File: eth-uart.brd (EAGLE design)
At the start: 52 x 21 mm, 41 parts, among them IC1 STM32F407VE, IC2 DP83848, IC3 LDS3985M33R, X5 USBMICRO_B, X7 B78477P1001A314

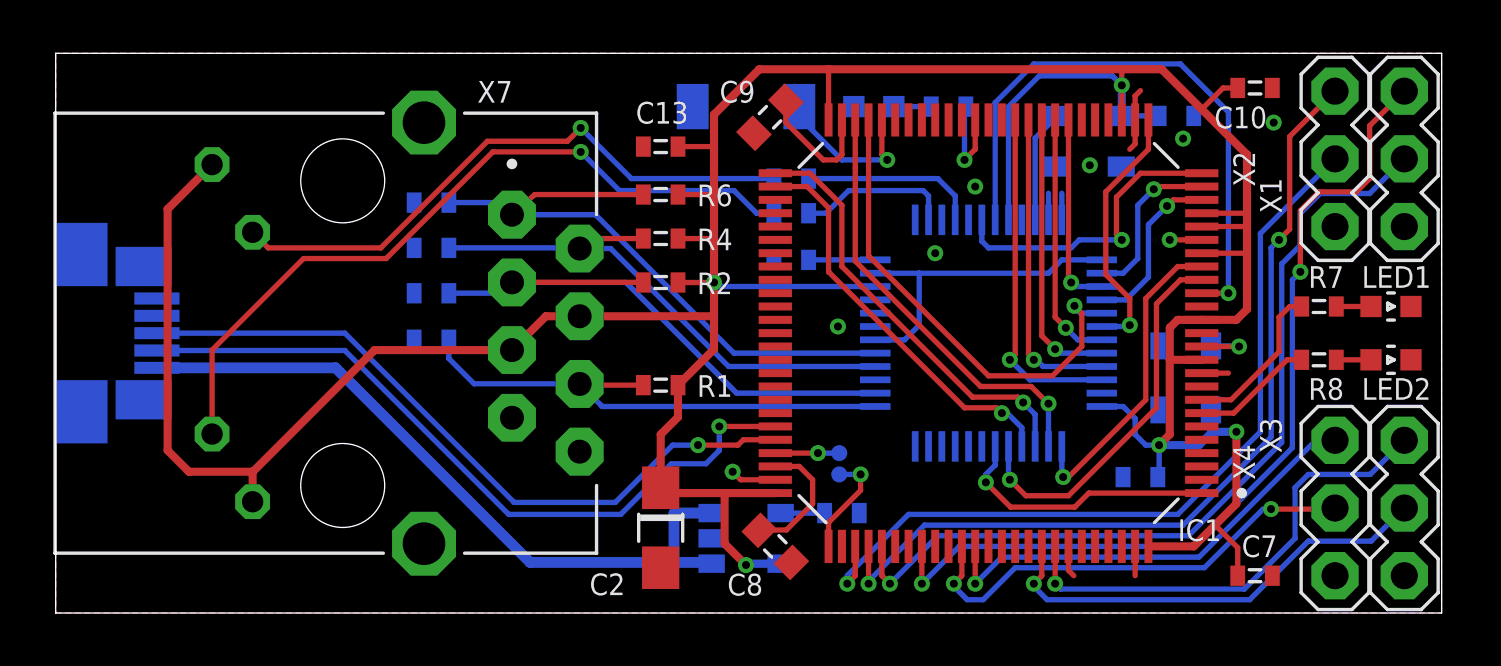
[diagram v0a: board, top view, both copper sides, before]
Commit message: boot0 on solidjump
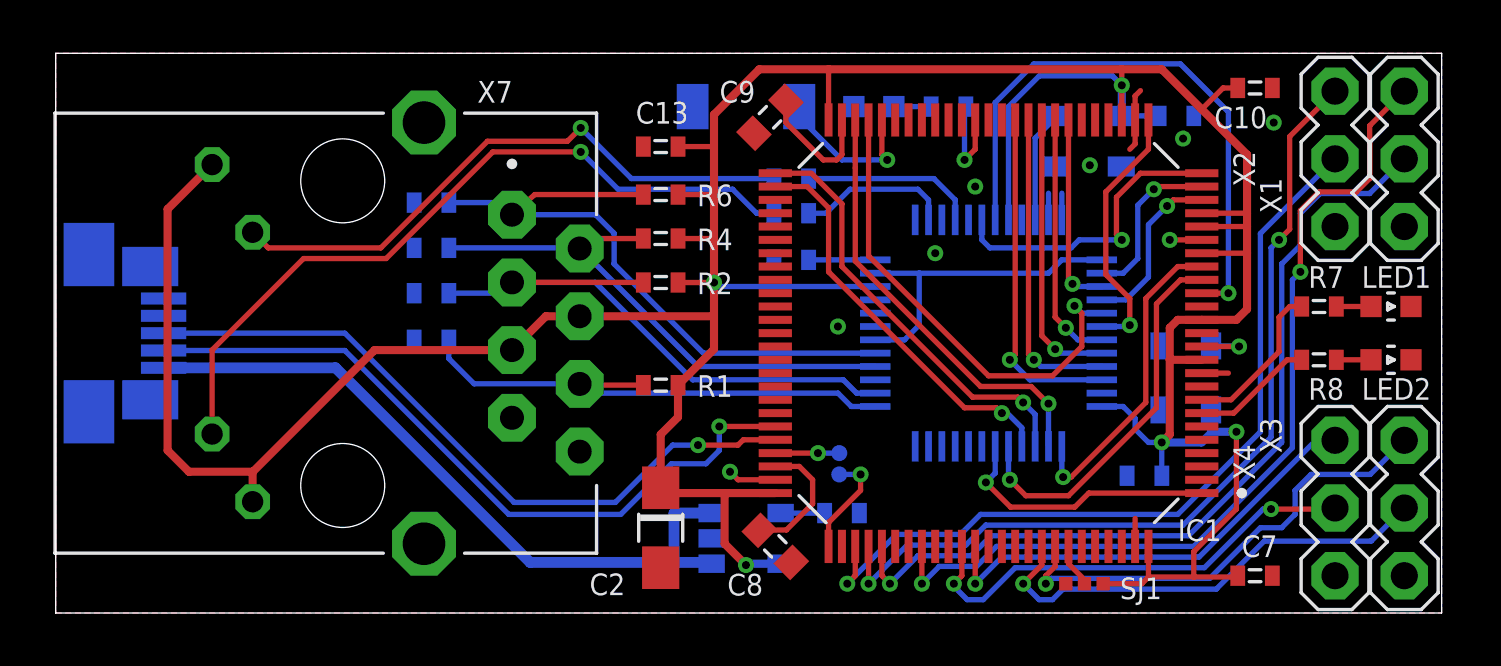
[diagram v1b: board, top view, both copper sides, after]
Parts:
- added SJ1: (no value), netcat:SJ3
- moved X5 0.25 mm to (1.25, 10.5)
- moved C11 0.16 mm to (40.9, 5.15)
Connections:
- net N$1 renamed LED_G
- net N$10 renamed LED_Y
- net N$42 renamed LED_LINK
- net N$43 renamed LED_ACT
- new net BOOT0: IC1.94, SJ1.2
- net 3.3V: now also SJ1.3
- net GND: now also SJ1.1; no longer IC1.94
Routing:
- net 3.3V: track 147.3 -> 150.5 mm
- net BOOT0: track 0.00 -> 1.65 mm
- net GND: track 10.6 -> 9.44 mm
- net TXDP: track 23.6 -> 24.2 mm
- net UART1_TX: track 17.2 -> 17.7 mm

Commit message: changed eth socket to HR911105A
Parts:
- X7: device netcat:B78477P1001A014 -> netcat:HR911105A
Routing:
- net LED_G: track 22.5 -> 24.0 mm
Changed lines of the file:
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@@
 <drawing>
 <settings>
-<setting alwaysvectorfont="yes"/>
+<setting alwaysvectorfont="no"/>
 <setting keepoldvectorfont="yes"/>
 <setting verticaltext="up"/>
@@
 <layer number="59" name="tCarbon" color="7" fill="1" visible="no" active="no"/>
 <layer number="60" name="bCarbon" color="7" fill="1" visible="no" active="no"/>
+<layer number="88" name="SimResults" color="9" fill="1" visible="no" active="no"/>
+<layer number="89" name="SimProbes" color="9" fill="1" visible="no" active="no"/>
 <layer number="90" name="Modules" color="7" fill="1" visible="no" active="no"/>
 <layer number="91" name="Nets" color="2" fill="1" visible="no" active="no"/>
@@
 <attribute name="VALUE" x="28.235" y="12.968" size="0.8128" layer="28" font="vector" rot="MR0"/>
 </element>
-<element name="X7" library="netcat" package="B78477P1001A014" value="B78477P1001A314" x="9.5" y="10.5" smashed="yes" rot="R270">
+<element name="X7" library="netcat" package="HR911105A" value="B78477P1001A314" x="9.5" y="10.5" smashed="yes" rot="R270">
 <attribute name="NAME" x="15.82" y="19.15" size="0.8128" layer="25" font="vector"/>
 <attribute name="VALUE" x="1.88" y="15.58" size="0.8128" layer="27" font="vector" rot="R270"/>
@@
 <wire x1="19.66" y1="11.135" x2="24.635" y2="11.135" width="0.3048" layer="1"/>
 <wire x1="24.635" y1="11.135" x2="24.7" y2="11.2" width="0.3048" layer="1"/>
-<wire x1="4.2" y1="15.155" x2="5.87" y2="16.825" width="0.3048" layer="1"/>
-<wire x1="11.965" y1="9.865" x2="17.12" y2="9.865" width="0.3048" layer="1"/>
-<wire x1="7.39" y1="5.29" x2="11.965" y2="9.865" width="0.3048" layer="1"/>
 <wire x1="17.12" y1="9.865" x2="18.39" y2="11.135" width="0.3048" layer="1"/>
 <wire x1="18.39" y1="11.135" x2="19.66" y2="11.135" width="0.3048" layer="1"/>
-<wire x1="7.39" y1="5.29" x2="7.39" y2="4.175" width="0.3048" layer="1"/>
-<wire x1="7.39" y1="5.29" x2="7.38" y2="5.3" width="0.3048" layer="1"/>
-<wire x1="7.38" y1="5.3" x2="5" y2="5.3" width="0.3048" layer="1"/>
-<wire x1="5" y1="5.3" x2="4.2" y2="6.1" width="0.3048" layer="1"/>
-<wire x1="4.2" y1="6.1" x2="4.2" y2="15.155" width="0.3048" layer="1"/>
 <wire x1="29" y1="18.5" x2="29" y2="20.4" width="0.2" layer="1"/>
 <wire x1="43" y1="15" x2="44.7" y2="15" width="0.2" layer="1"/>
@@
 <wire x1="41" y1="1.35" x2="42.7" y2="1.35" width="0.2" layer="1"/>
 <wire x1="41" y1="2.5" x2="41" y2="1.35" width="0.2" layer="1"/>
+<wire x1="17.12" y1="9.865" x2="11.56" y2="9.865" width="0.2" layer="1"/>
+<wire x1="11.56" y1="9.865" x2="5.87" y2="4.175" width="0.2" layer="1"/>
+<wire x1="5.87" y1="16.825" x2="4.3" y2="15.255" width="0.2" layer="1"/>
+<wire x1="4.3" y1="5.745" x2="5.87" y2="4.175" width="0.2" layer="1"/>
+<wire x1="4.3" y1="15.255" x2="4.3" y2="5.745" width="0.2" layer="1"/>
 </signal>
 <signal name="LED_G">
 <contactref element="X7" pad="10"/>
 <contactref element="R3" pad="2"/>
-<wire x1="7.39" y1="14.285" x2="7.975" y2="13.7" width="0.2" layer="1"/>
-<wire x1="7.975" y1="13.7" x2="12.2" y2="13.7" width="0.2" layer="1"/>
 <via x="19.7" y="18.2" extent="1-16" drill="0.3" shape="octagon"/>
-<wire x1="12.2" y1="13.7" x2="16.2" y2="17.7" width="0.2" layer="1"/>
+<wire x1="16.2" y1="17.7" x2="12.2" y2="13.7" width="0.2" layer="1"/>
 <wire x1="19.2" y1="17.7" x2="19.7" y2="18.2" width="0.2" layer="1"/>
 <wire x1="16.2" y1="17.7" x2="19.2" y2="17.7" width="0.2" layer="1"/>
 <wire x1="19.7" y1="18.2" x2="21.6" y2="16.3" width="0.2" layer="16"/>
 <wire x1="21.6" y1="16.3" x2="26.95" y2="16.3" width="0.2" layer="16"/>
+<wire x1="12.2" y1="13.7" x2="6.455" y2="13.7" width="0.2" layer="1"/>
+<wire x1="6.455" y1="13.7" x2="5.87" y2="14.285" width="0.2" layer="1"/>
 </signal>
 <signal name="LED_Y">

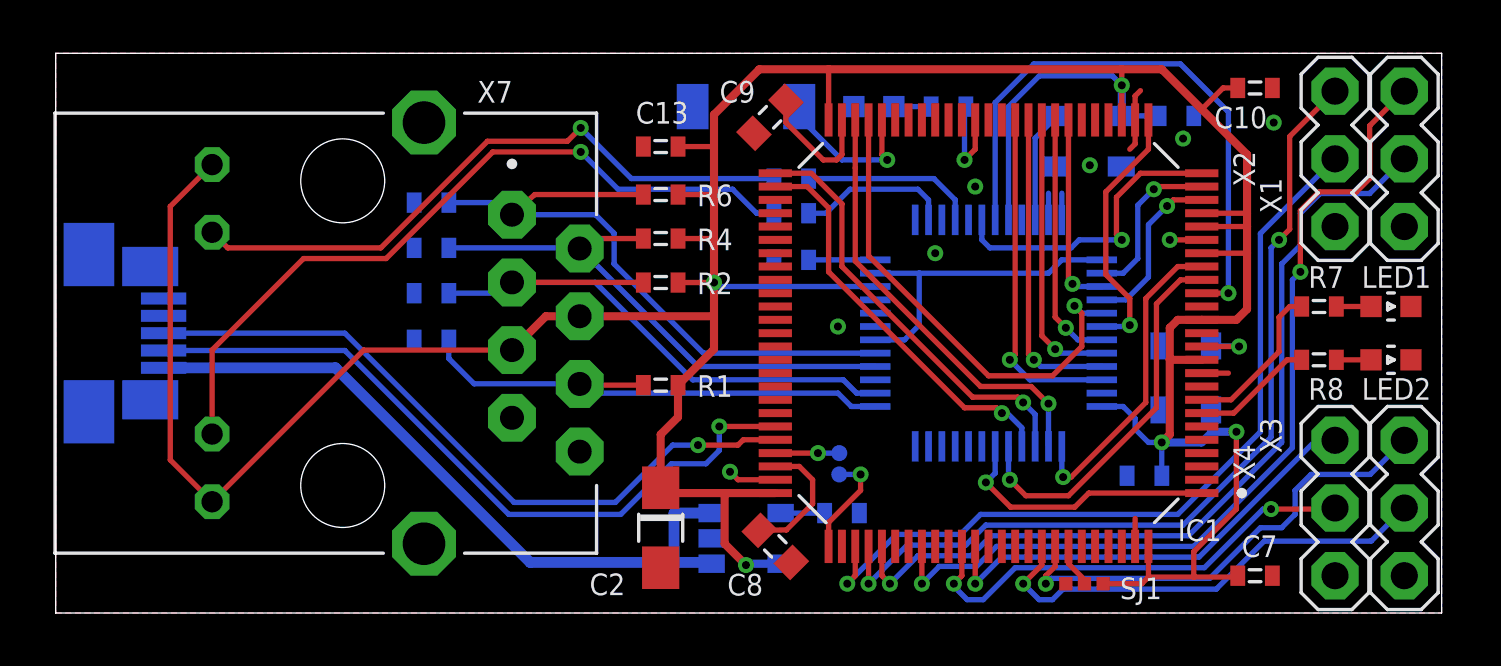
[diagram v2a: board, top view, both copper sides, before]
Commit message: added solid jumper for RMII/MII clock selecting
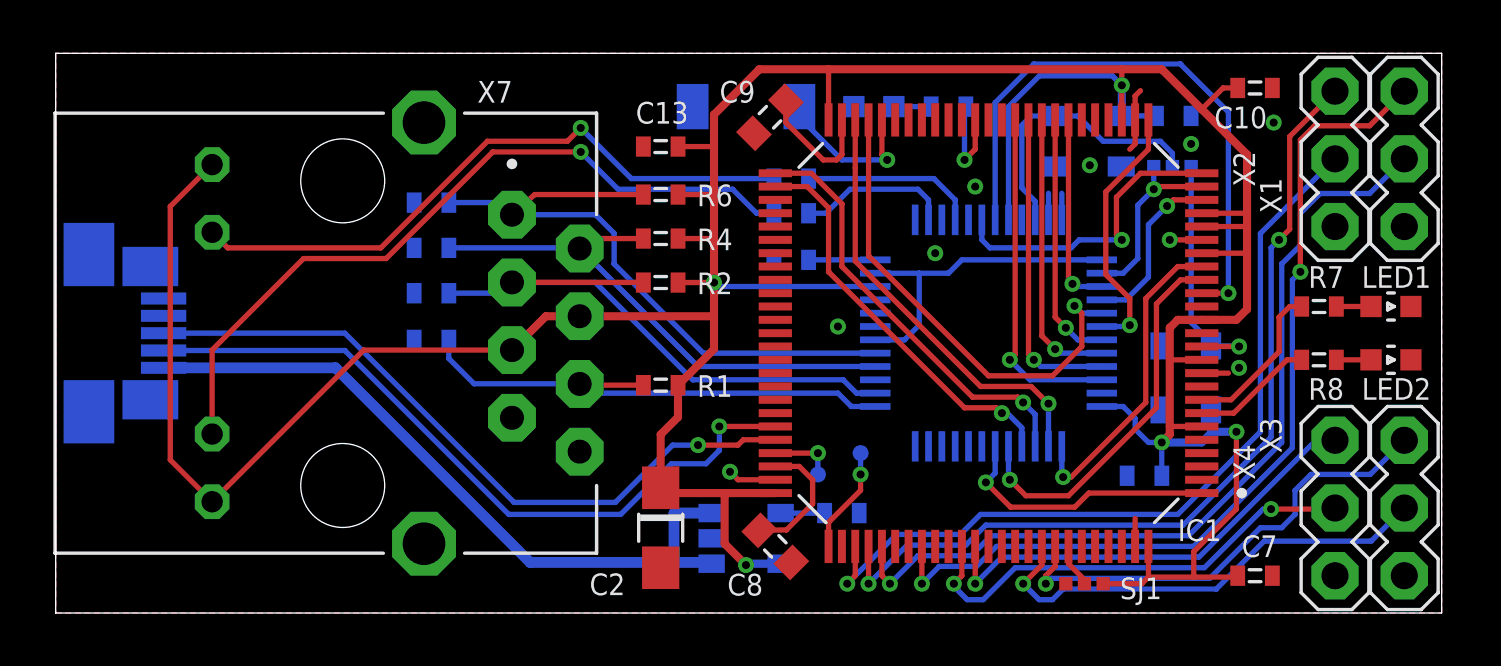
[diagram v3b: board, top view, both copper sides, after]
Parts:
- added SJ2: (no value), netcat:SJ3
- OSC1: value 25mhz -> 8mhz
- OSC2: value 8mhz -> 25mhz
- TP2: value C -> CLK
- moved U$1 15.4 mm to (9.30, 10.4)
- moved OSC1 9.55 mm to (42.4, 8.90), turned to 90 degrees
- moved OSC2 9.55 mm to (38.7, 17.7), turned to 0 degrees
- moved TP2 1.13 mm to (30.2, 6.00)
- moved TP1 1.13 mm to (28.6, 5.20)
- moved C12 0.10 mm to (42.0, 18.6)
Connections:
- removed net N$3: IC2.34, OSC1.3
- new net PHY_OSC: IC2.34, OSC2.3, SJ2.2
- net 3.3V: now also IC1.6
- net ETH_RX_CLK: now also SJ2.3
- net SYS_CLK: now also OSC1.3, SJ2.1; no longer OSC2.3
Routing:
- net PHY_OSC: track 0.00 -> 10.8 mm
- net SYS_CLK: track 2.46 -> 9.50 mm
- net N$3: track 4.24 -> 0.00 mm
- net 3.3V: track 150.4 -> 151.5 mm
- net ETH_RX_CLK: track 6.27 -> 7.12 mm
- net GND: vias 8 -> 9
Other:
- board text added: "MII"
- board text added: "RMII"
